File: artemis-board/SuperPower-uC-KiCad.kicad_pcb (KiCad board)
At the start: 4 copper layers, 45.1 x 45.1 mm, 96 parts, among them J1 Battery connector, J10 External NTC, J2 Thermistor, J3 USB_B_Micro, J4 Solar in, J8 regulator board, Q1 2N7002, Q10 AO3401A, Q11 2N7002, Q2 2N7002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

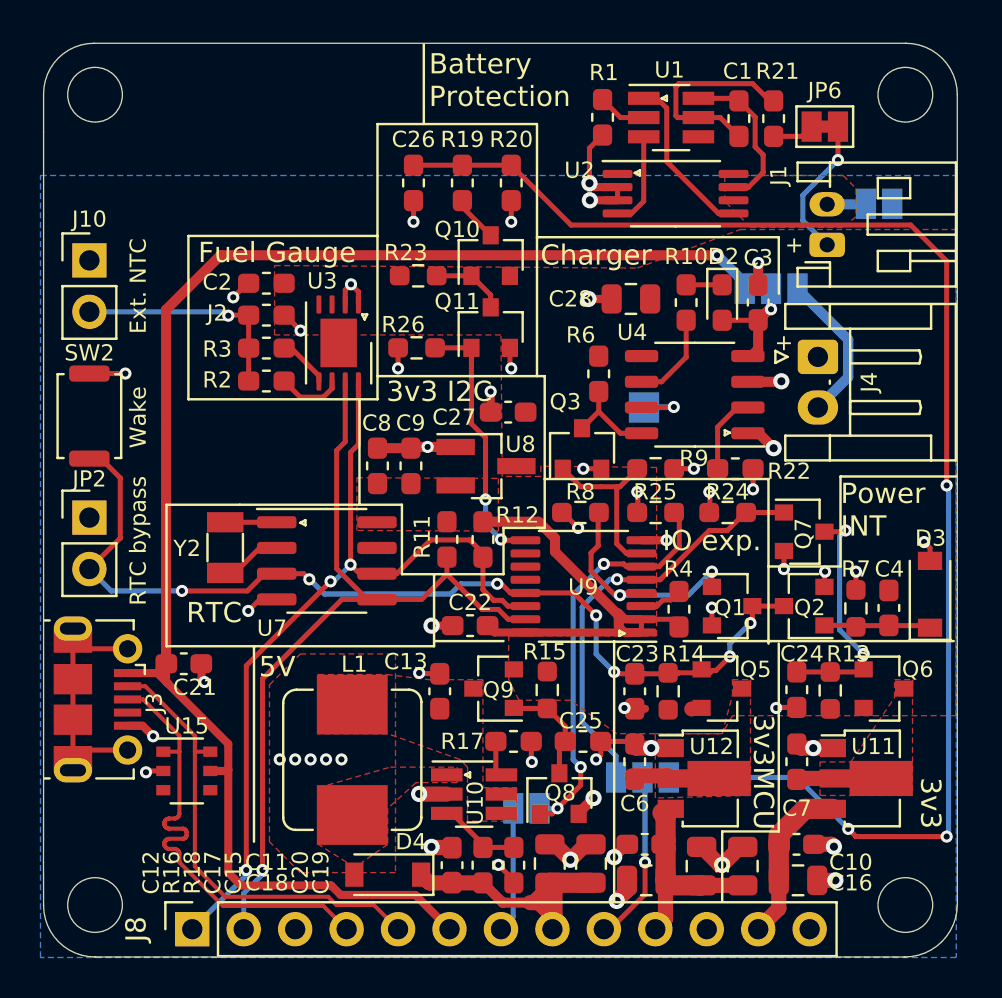
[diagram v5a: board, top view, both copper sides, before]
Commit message: added cap to 3v3 I2c, swapped some footprints to normal...
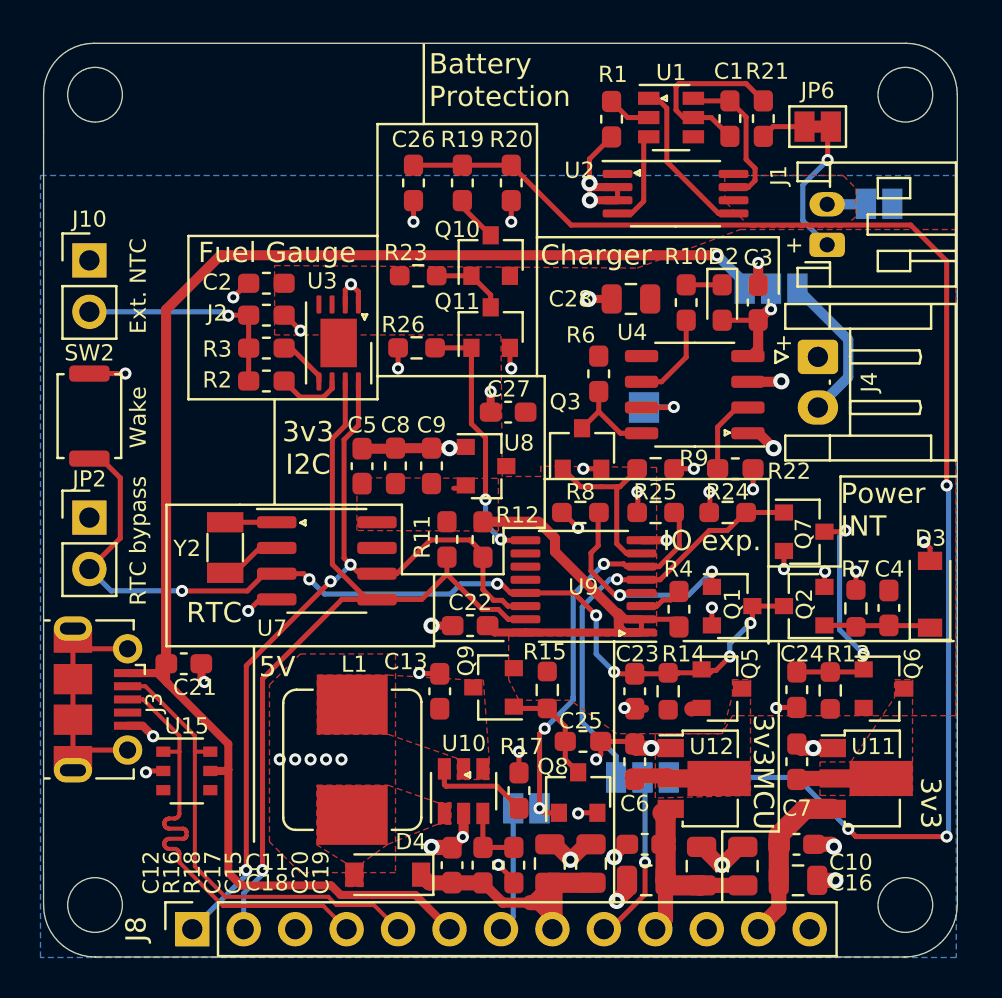
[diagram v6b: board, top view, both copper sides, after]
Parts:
- added C5: 1µF, Capacitor_SMD:C_0603_1608Metric_Pad1.08x0.95mm_HandSolder, F.Cu at (148.9, 99.2)
- U1, U10: footprint Package_TO_SOT_SMD:SOT-23-6_Handsoldering -> Package_TO_SOT_SMD:SOT-23-6
- U8: footprint Package_TO_SOT_SMD:SOT-23_Handsoldering -> Package_TO_SOT_SMD:SOT-23
- moved R17 2.44 mm to (156.7, 115.2), turned to 90 degrees
- moved C9 1.02 mm to (152.4, 99.2)
- moved Q8 0.93 mm to (159.6, 115.3)
- moved C8 0.89 mm to (150.6, 99.2)
- moved U10 0.54 mm to (154.0, 115.2), turned to 90 degrees
- moved R21 0.51 mm to (168.8, 82.0)
- moved R1 0.45 mm to (161.3, 82.1)
- moved C1 0.44 mm to (167.1, 82.0)
- moved JP6 0.35 mm to (171.4, 82.4)
- moved Q9 0.06 mm to (155.4, 110.1)
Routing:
- net Net-(R17-Pad1): track 1.77 -> 4.95 mm
- net GND: track 70.5 -> 72.3 mm
- net Net-(C1-Pad1): track 10.2 -> 9.08 mm
- net /RTC and Cut-Off Module/5V_EN: track 21.2 -> 20.4 mm
- net Net-(R16-Pad2): track 4.10 -> 3.36 mm

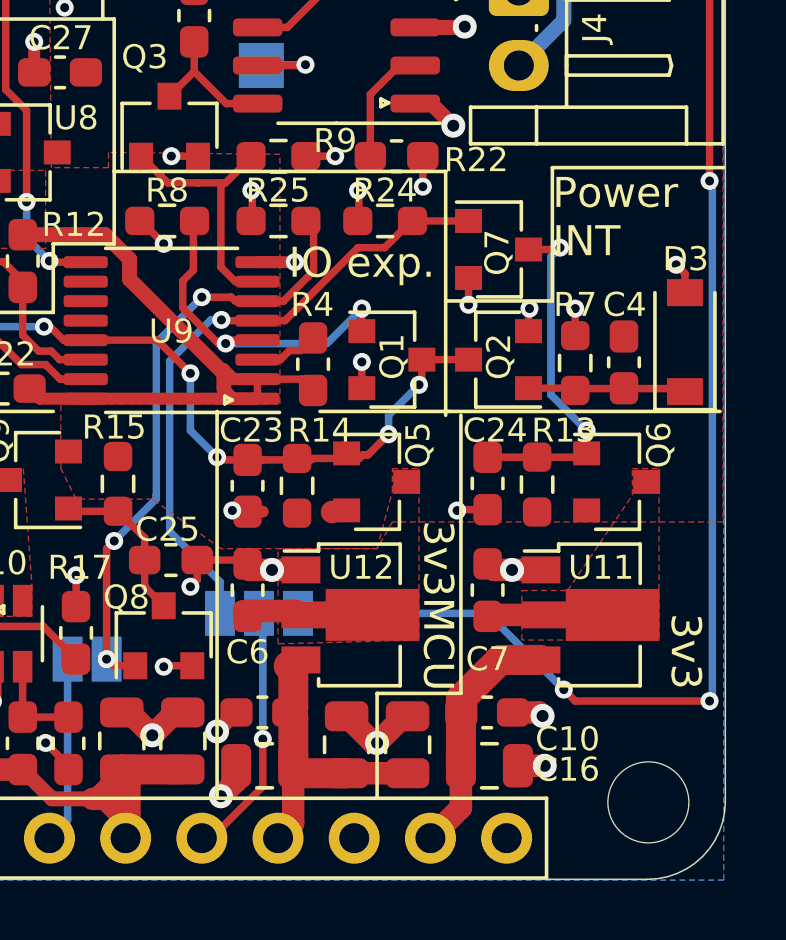
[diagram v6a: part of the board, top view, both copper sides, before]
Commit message: improved silk placement and routing
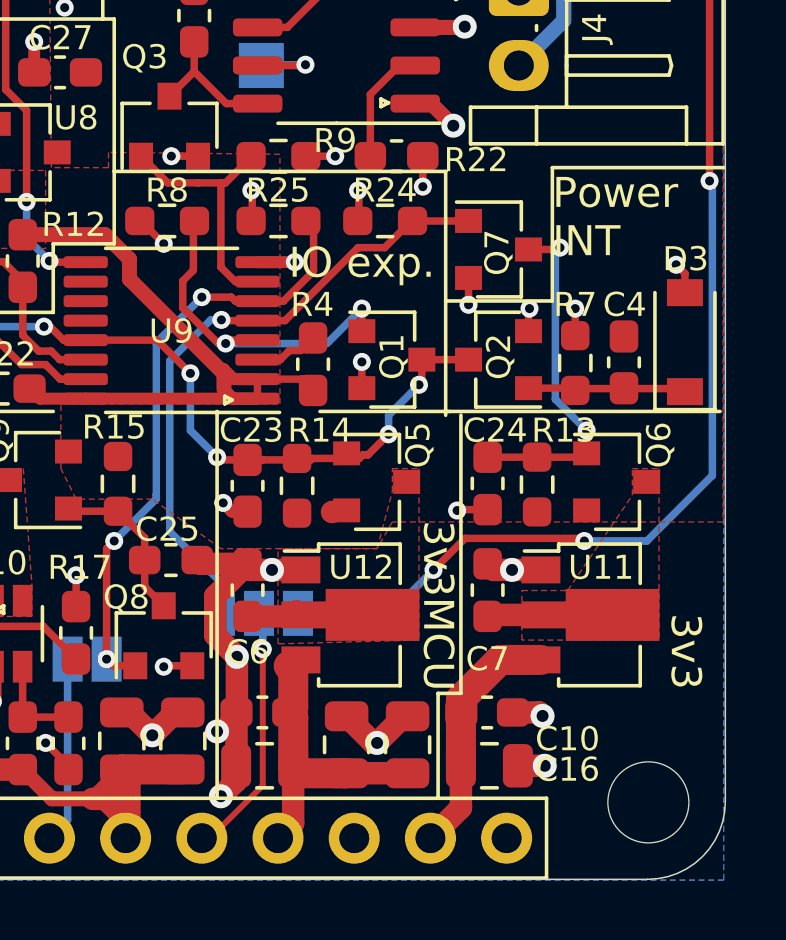
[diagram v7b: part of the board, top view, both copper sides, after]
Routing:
- net /RTC and Cut-Off Module/Vmeasure: track 71.7 -> 65.0 mm
- net GND: track 72.3 -> 78.7 mm

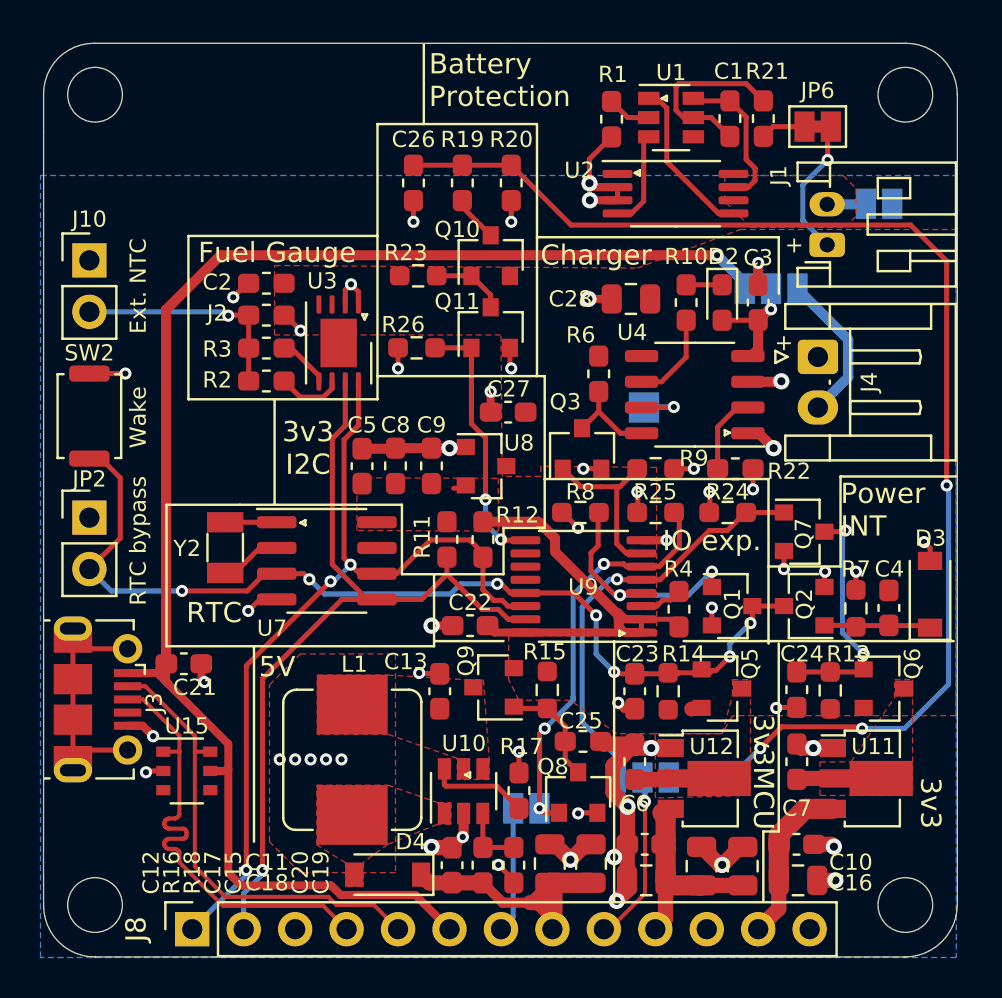
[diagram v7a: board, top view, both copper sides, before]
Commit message: added PCA9557 and swapped IO expander for it
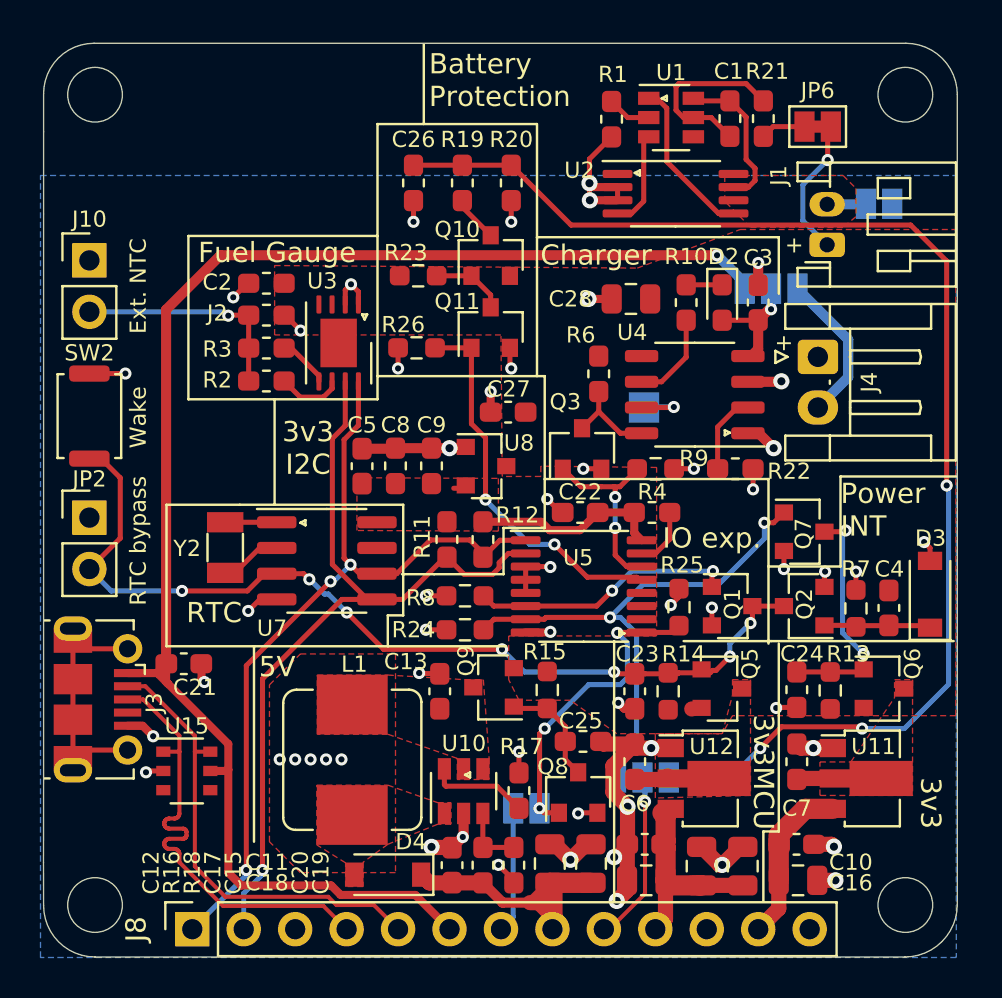
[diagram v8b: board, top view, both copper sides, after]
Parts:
- removed U9: TCA6408A, Package_SO:TSSOP-16_4.4x5mm_P0.65mm
- added U5: PCA9557PW, Package_SO:TSSOP-16_4.4x5mm_P0.65mm, F.Cu at (159.9, 105.1)
- moved R24 14.2 mm to (154.0, 107.3)
- moved C22 7.79 mm to (159.7, 101.5)
- moved R8 7.03 mm to (154.0, 105.6)
- moved R4 4.96 mm to (163.3, 101.5), turned to 180 degrees
- moved R25 4.82 mm to (164.6, 106.1), turned to 90 degrees
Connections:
- R4 pad 1: /Charging Module/3v3_I2C -> Net-(R4-Pad1)
- R4 pad 2: Net-(R4-Pad2) -> /Charging Module/3v3_I2C
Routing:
- net /Charging Module/3v3_I2C: track 24.2 -> 9.87 mm
- net Net-(Q11-Pad1): track 13.2 -> 19.0 mm
- net /RTC and Cut-Off Module/3v3V_EN: track 21.0 -> 26.9 mm, vias 1 -> 2
- net /RTC and Cut-Off Module/5V_EN: track 20.4 -> 15.8 mm
- net Net-(R4-Pad1): track 0.00 -> 3.00 mm
- net GND: track 78.7 -> 81.1 mm, vias 55 -> 56
- net Net-(R4-Pad2): track 2.22 -> 0.00 mm
- net /SCL: track 43.7 -> 41.9 mm
- net /Charging Module/INT: track 47.9 -> 46.4 mm
- net /RTC and Cut-Off Module/~INT: track 11.8 -> 13.1 mm
- net /RTC and Cut-Off Module/~CH_DIS: track 8.67 -> 9.38 mm, vias 0 -> 2
